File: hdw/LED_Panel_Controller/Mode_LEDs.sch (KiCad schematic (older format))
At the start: 0 parts

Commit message: made a lot more schematic progress
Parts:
- added C? (x9): 0.1uF, Capacitors_SMD:C_0402, symbol Custom_Library:C_Custom
- added D? (x9): Green, LEDs:LED_0402, symbol Device:LED
- added R? (x9): 1k, Resistors_SMD:R_0402, symbol Custom_Library:R_Custom
- added R? (x9): 10k, Resistors_SMD:R_0402, symbol Custom_Library:R_Custom
- added U? (x9): 74LVC1G97, Package_TO_SOT_SMD:SOT-363_SC-70-6, symbol Custom_Library:74LVC1G97_Power_NOT
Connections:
- new net: D?.1 (K), U?.4 (x9)
- new net: D?.2 (A), R?.2 (x9)
- new net +3V3: C?.1, C?.1, C?.1, C?.1, C?.1, C?.1, C?.1, C?.1, C?.1, R?.1, R?.1, R?.1, R?.1, R?.1, R?.1, R?.1, R?.1, R?.1, U?.1 (VCC), U?.1 (VCC), U?.1 (VCC), U?.1 (VCC), U?.1 (VCC), U?.1 (VCC), U?.1 (VCC), U?.1 (VCC), U?.1 (VCC), U?.5 (VCC), U?.5 (VCC), U?.5 (VCC), U?.5 (VCC), U?.5 (VCC), U?.5 (VCC), U?.5 (VCC), U?.5 (VCC), U?.5 (VCC)
- new net Clock_Mode_LED: R?.1, U?.6
- new net Flash_Slideshow_Mode_LED: R?.1, U?.6
- new net GND: C?.2, C?.2, C?.2, C?.2, C?.2, C?.2, C?.2, C?.2, C?.2, R?.2, R?.2, R?.2, R?.2, R?.2, R?.2, R?.2, R?.2, R?.2, U?.2 (GND), U?.2 (GND), U?.2 (GND), U?.2 (GND), U?.2 (GND), U?.2 (GND), U?.2 (GND), U?.2 (GND), U?.2 (GND), U?.3 (GND), U?.3 (GND), U?.3 (GND), U?.3 (GND), U?.3 (GND), U?.3 (GND), U?.3 (GND), U?.3 (GND), U?.3 (GND)
- new net Prog1_Mode_LED: R?.1, U?.6
- new net Prog2_Mode_LED: R?.1, U?.6
- new net Prog3_Mode_LED: R?.1, U?.6
- new net Prog4_Mode_LED: R?.1, U?.6
- new net Prog5_Mode_LED: R?.1, U?.6
- new net Prog6_Mode_LED: R?.1, U?.6
- new net USB_Stream_Mode_LED: R?.1, U?.6

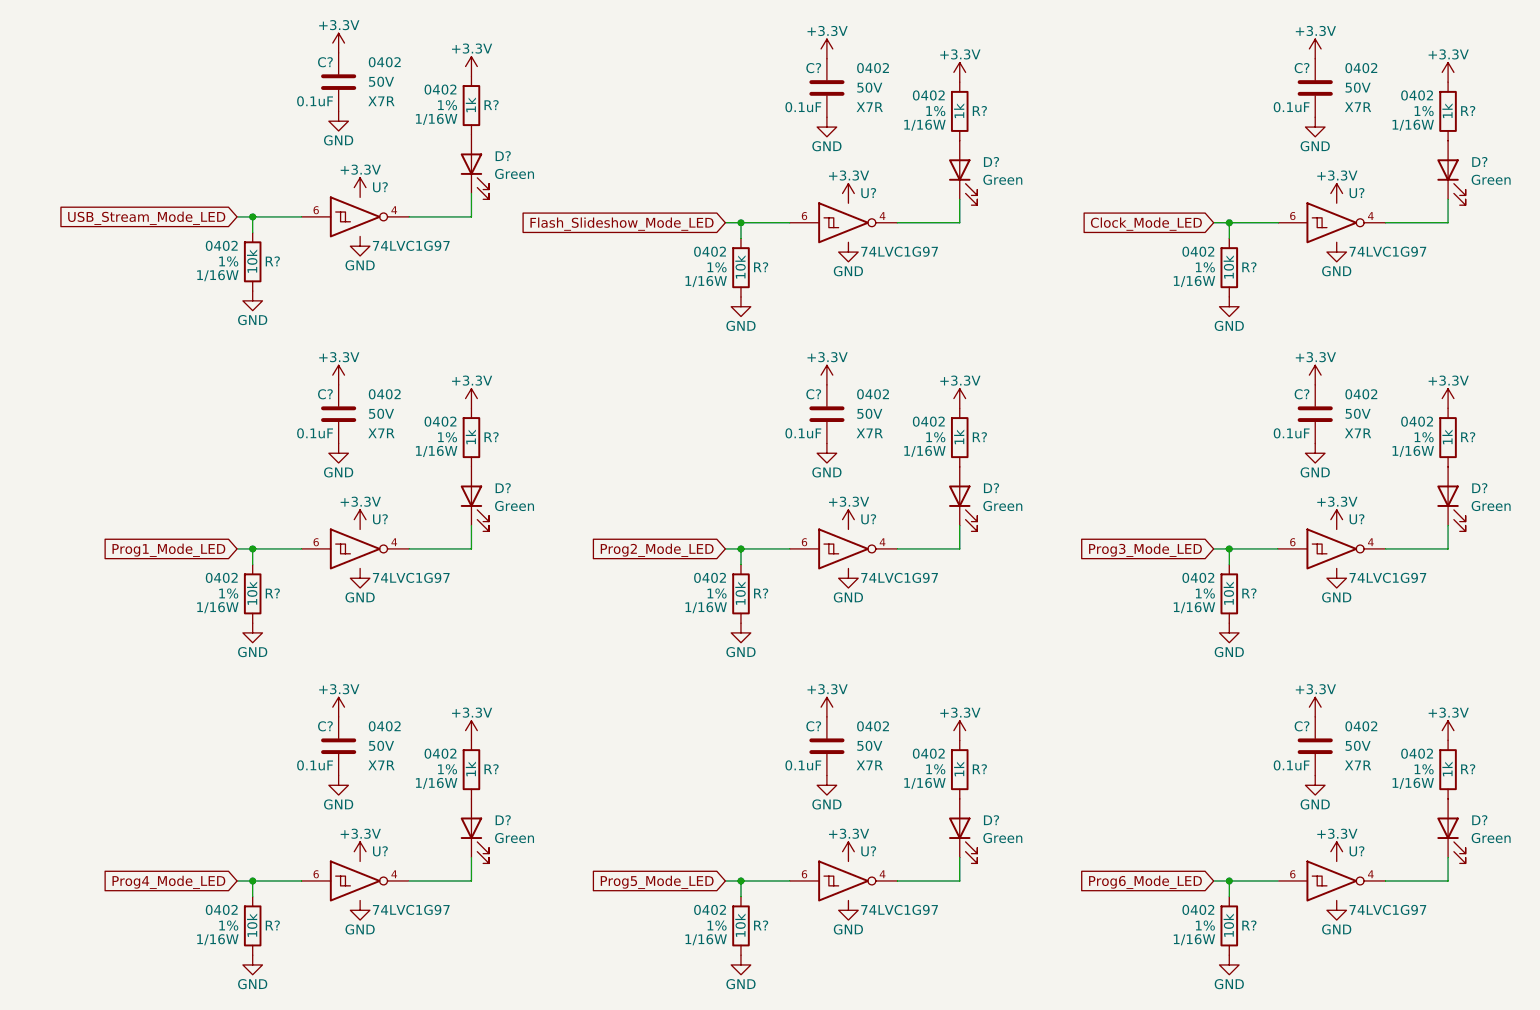
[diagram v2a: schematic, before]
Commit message: assigned a lot of nets to MCU pins
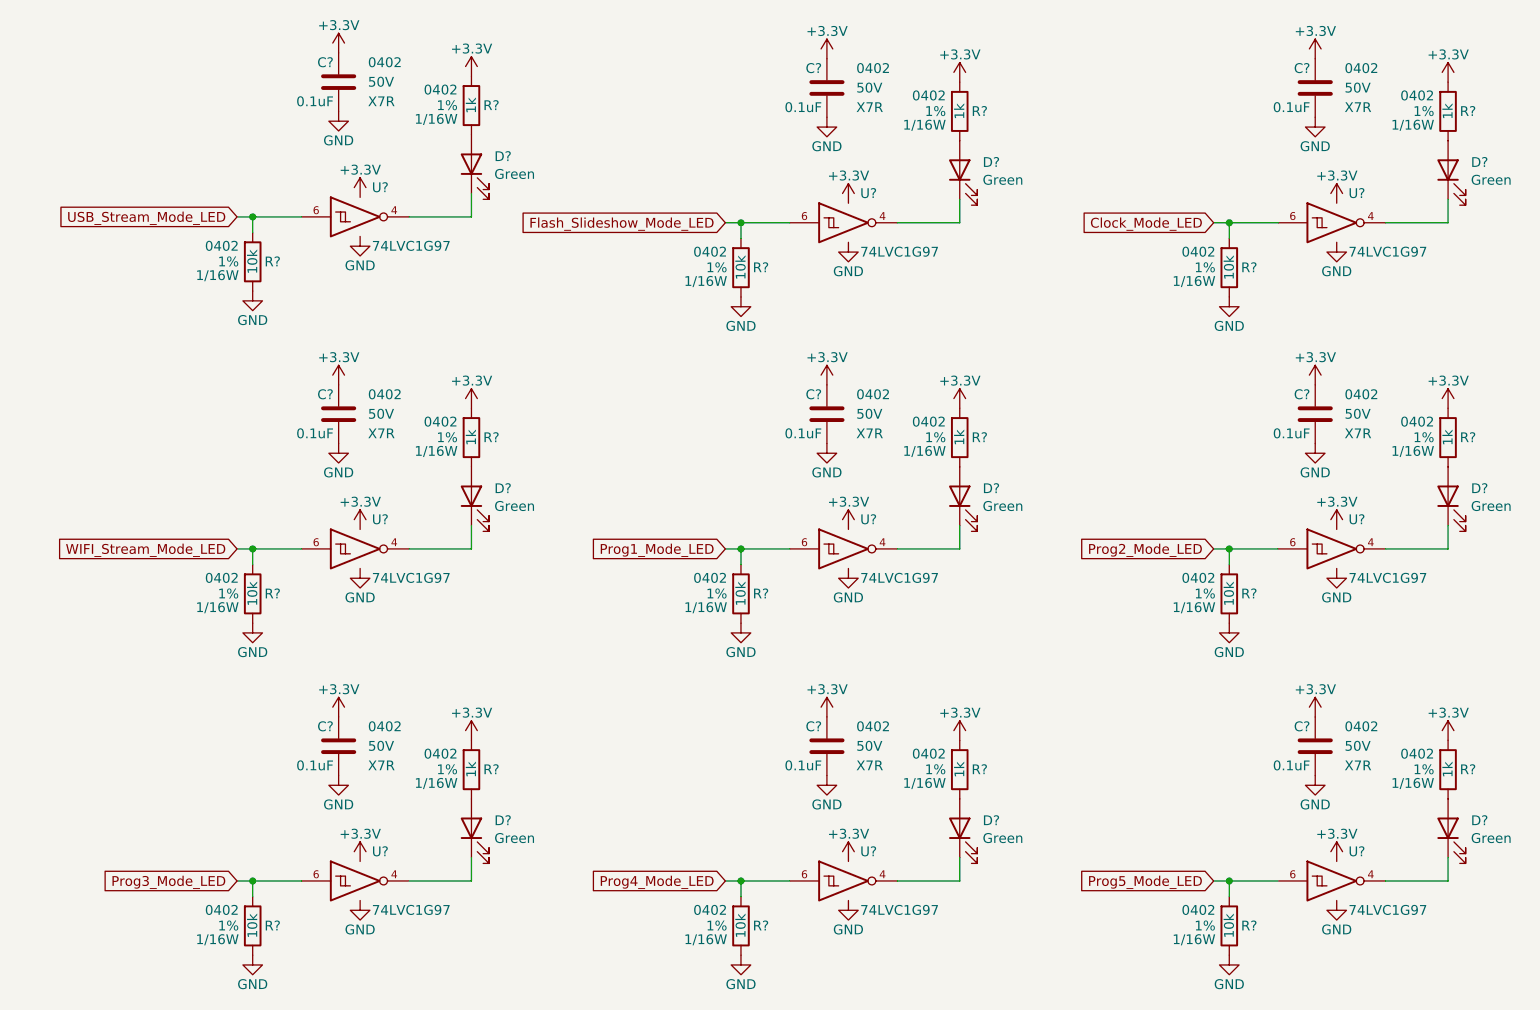
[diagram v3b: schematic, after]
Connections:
- net Prog6_Mode_LED is gone; now on net Prog5_Mode_LED: R?.1, U?.6
- net Prog1_Mode_LED: now also R?.1, U?.6; no longer R?.1, U?.6
- net Prog2_Mode_LED: now also R?.1, U?.6; no longer R?.1, U?.6
- net Prog3_Mode_LED: now also R?.1, U?.6; no longer R?.1, U?.6
- net Prog4_Mode_LED: now also R?.1, U?.6; no longer R?.1, U?.6
- net Prog5_Mode_LED: no longer R?.1, U?.6
- new net WIFI_Stream_Mode_LED: R?.1, U?.6
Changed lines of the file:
@@
 $EndComp
 Text GLabel 1560 3460 0    50   Input ~ 0
-Prog1_Mode_LED
+WIFI_Stream_Mode_LED
 $Comp
 L Custom_Library:C_Custom C?
@@
 $EndComp
 Text GLabel 4060 3460 0    50   Input ~ 0
-Prog2_Mode_LED
+Prog1_Mode_LED
 $Comp
 L Custom_Library:C_Custom C?
@@
 $EndComp
 Text GLabel 6560 3460 0    50   Input ~ 0
-Prog3_Mode_LED
+Prog2_Mode_LED
 $Comp
 L Custom_Library:C_Custom C?
@@
 $EndComp
 Text GLabel 1560 5160 0    50   Input ~ 0
-Prog4_Mode_LED
+Prog3_Mode_LED
 $Comp
 L Custom_Library:C_Custom C?
@@
 $EndComp
 Text GLabel 4060 5160 0    50   Input ~ 0
-Prog5_Mode_LED
+Prog4_Mode_LED
 $Comp
 L Custom_Library:C_Custom C?
@@
 $EndComp
 Text GLabel 6560 5160 0    50   Input ~ 0
-Prog6_Mode_LED
+Prog5_Mode_LED
 $Comp
 L Custom_Library:C_Custom C?

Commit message: more schematic development
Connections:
- net Clock_Mode_LED renamed Void_Mode_LED
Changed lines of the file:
@@
 $Descr A 11000 8500
 encoding utf-8
-Sheet 22 34
+Sheet 23 34
 Title "LED Panel Controller"
-Date "2020-12-23"
+Date "2021-03-24"
 Rev "A"
-Comp "Drew Maatman, Logan Wedel"
+Comp "Drew Maatman"
 Comment1 ""
 Comment2 ""
@@
 	6640 1790 6640 1870
 Text GLabel 6560 1790 0    50   Input ~ 0
-Clock_Mode_LED
+Void_Mode_LED
 Wire Wire Line
 	6560 1790 6640 1790

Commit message: added digikey pns, footprints, bom scrubbed
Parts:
- R? (x9): Digi-Key PN (none) -> RMCF0402FT1K00CT-ND
- U? (x9): Digi-Key PN (none) -> 1727-1772-1-ND
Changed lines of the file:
@@
 F 5 "1%" H 2830 1190 50  0000 L CNN "Tolerance"
 F 6 "1/16W" H 2830 1120 50  0000 L CNN "Wattage"
-F 7 "" H 3060 1590 60  0001 C CNN "Digi-Key PN"
+F 7 "RMCF0402FT1K00CT-ND" H 3060 1590 60  0001 C CNN "Digi-Key PN"
 	1    2760 1190
 	-1   0    0    -1
@@
 F 2 "Package_TO_SOT_SMD:SOT-363_SC-70-6" H 2240 1760 50  0001 C CNN
 F 3 "http://www.ti.com/lit/ds/symlink/sn74lvc1g97.pdf" H 2240 1760 50  0001 C CNN
+F 4 "1727-1772-1-ND" H 2190 1760 50  0001 C CNN "Digi-Key PN"
 	1    2190 1760
 	1    0    0    -1
@@
 F 5 "1%" H 5330 1220 50  0000 L CNN "Tolerance"
 F 6 "1/16W" H 5330 1150 50  0000 L CNN "Wattage"
-F 7 "" H 5560 1620 60  0001 C CNN "Digi-Key PN"
+F 7 "RMCF0402FT1K00CT-ND" H 5560 1620 60  0001 C CNN "Digi-Key PN"
 	1    5260 1220
 	-1   0    0    -1
@@
 F 2 "Package_TO_SOT_SMD:SOT-363_SC-70-6" H 4740 1790 50  0001 C CNN
 F 3 "http://www.ti.com/lit/ds/symlink/sn74lvc1g97.pdf" H 4740 1790 50  0001 C CNN
+F 4 "1727-1772-1-ND" H 4690 1790 50  0001 C CNN "Digi-Key PN"
 	1    4690 1790
 	1    0    0    -1
@@
 F 5 "1%" H 2830 2890 50  0000 L CNN "Tolerance"
 F 6 "1/16W" H 2830 2820 50  0000 L CNN "Wattage"
-F 7 "" H 3060 3290 60  0001 C CNN "Digi-Key PN"
+F 7 "RMCF0402FT1K00CT-ND" H 3060 3290 60  0001 C CNN "Digi-Key PN"
 	1    2760 2890
 	-1   0    0    -1
@@
 F 2 "Package_TO_SOT_SMD:SOT-363_SC-70-6" H 2240 3460 50  0001 C CNN
 F 3 "http://www.ti.com/lit/ds/symlink/sn74lvc1g97.pdf" H 2240 3460 50  0001 C CNN
+F 4 "1727-1772-1-ND" H 2190 3460 50  0001 C CNN "Digi-Key PN"
 	1    2190 3460
 	1    0    0    -1
@@
 F 5 "1%" H 5330 2890 50  0000 L CNN "Tolerance"
 F 6 "1/16W" H 5330 2820 50  0000 L CNN "Wattage"
-F 7 "" H 5560 3290 60  0001 C CNN "Digi-Key PN"
+F 7 "RMCF0402FT1K00CT-ND" H 5560 3290 60  0001 C CNN "Digi-Key PN"
 	1    5260 2890
 	-1   0    0    -1
@@
 F 2 "Package_TO_SOT_SMD:SOT-363_SC-70-6" H 4740 3460 50  0001 C CNN
 F 3 "http://www.ti.com/lit/ds/symlink/sn74lvc1g97.pdf" H 4740 3460 50  0001 C CNN
+F 4 "1727-1772-1-ND" H 4690 3460 50  0001 C CNN "Digi-Key PN"
 	1    4690 3460
 	1    0    0    -1
@@
 F 5 "1%" H 7830 2890 50  0000 L CNN "Tolerance"
 F 6 "1/16W" H 7830 2820 50  0000 L CNN "Wattage"
-F 7 "" H 8060 3290 60  0001 C CNN "Digi-Key PN"
+F 7 "RMCF0402FT1K00CT-ND" H 8060 3290 60  0001 C CNN "Digi-Key PN"
 	1    7760 2890
 	-1   0    0    -1
@@
 F 2 "Package_TO_SOT_SMD:SOT-363_SC-70-6" H 7240 3460 50  0001 C CNN
 F 3 "http://www.ti.com/lit/ds/symlink/sn74lvc1g97.pdf" H 7240 3460 50  0001 C CNN
+F 4 "1727-1772-1-ND" H 7190 3460 50  0001 C CNN "Digi-Key PN"
 	1    7190 3460
 	1    0    0    -1
@@
 F 5 "1%" H 2830 4590 50  0000 L CNN "Tolerance"
 F 6 "1/16W" H 2830 4520 50  0000 L CNN "Wattage"
-F 7 "" H 3060 4990 60  0001 C CNN "Digi-Key PN"
+F 7 "RMCF0402FT1K00CT-ND" H 3060 4990 60  0001 C CNN "Digi-Key PN"
 	1    2760 4590
 	-1   0    0    -1
@@
 F 2 "Package_TO_SOT_SMD:SOT-363_SC-70-6" H 2240 5160 50  0001 C CNN
 F 3 "http://www.ti.com/lit/ds/symlink/sn74lvc1g97.pdf" H 2240 5160 50  0001 C CNN
+F 4 "1727-1772-1-ND" H 2190 5160 50  0001 C CNN "Digi-Key PN"
 	1    2190 5160
 	1    0    0    -1
@@
 F 5 "1%" H 5330 4590 50  0000 L CNN "Tolerance"
 F 6 "1/16W" H 5330 4520 50  0000 L CNN "Wattage"
-F 7 "" H 5560 4990 60  0001 C CNN "Digi-Key PN"
+F 7 "RMCF0402FT1K00CT-ND" H 5560 4990 60  0001 C CNN "Digi-Key PN"
 	1    5260 4590
 	-1   0    0    -1
@@
 F 2 "Package_TO_SOT_SMD:SOT-363_SC-70-6" H 4740 5160 50  0001 C CNN
 F 3 "http://www.ti.com/lit/ds/symlink/sn74lvc1g97.pdf" H 4740 5160 50  0001 C CNN
+F 4 "1727-1772-1-ND" H 4690 5160 50  0001 C CNN "Digi-Key PN"
 	1    4690 5160
 	1    0    0    -1
@@
 F 5 "1%" H 7830 4590 50  0000 L CNN "Tolerance"
 F 6 "1/16W" H 7830 4520 50  0000 L CNN "Wattage"
-F 7 "" H 8060 4990 60  0001 C CNN "Digi-Key PN"
+F 7 "RMCF0402FT1K00CT-ND" H 8060 4990 60  0001 C CNN "Digi-Key PN"
 	1    7760 4590
 	-1   0    0    -1
@@
 F 2 "Package_TO_SOT_SMD:SOT-363_SC-70-6" H 7240 5160 50  0001 C CNN
 F 3 "http://www.ti.com/lit/ds/symlink/sn74lvc1g97.pdf" H 7240 5160 50  0001 C CNN
+F 4 "1727-1772-1-ND" H 7190 5160 50  0001 C CNN "Digi-Key PN"
 	1    7190 5160
 	1    0    0    -1
@@
 F 5 "1%" H 7830 1220 50  0000 L CNN "Tolerance"
 F 6 "1/16W" H 7830 1150 50  0000 L CNN "Wattage"
-F 7 "" H 8060 1620 60  0001 C CNN "Digi-Key PN"
+F 7 "RMCF0402FT1K00CT-ND" H 8060 1620 60  0001 C CNN "Digi-Key PN"
 	1    7760 1220
 	-1   0    0    -1
@@
 F 2 "Package_TO_SOT_SMD:SOT-363_SC-70-6" H 7240 1790 50  0001 C CNN
 F 3 "http://www.ti.com/lit/ds/symlink/sn74lvc1g97.pdf" H 7240 1790 50  0001 C CNN
+F 4 "1727-1772-1-ND" H 7190 1790 50  0001 C CNN "Digi-Key PN"
 	1    7190 1790
 	1    0    0    -1

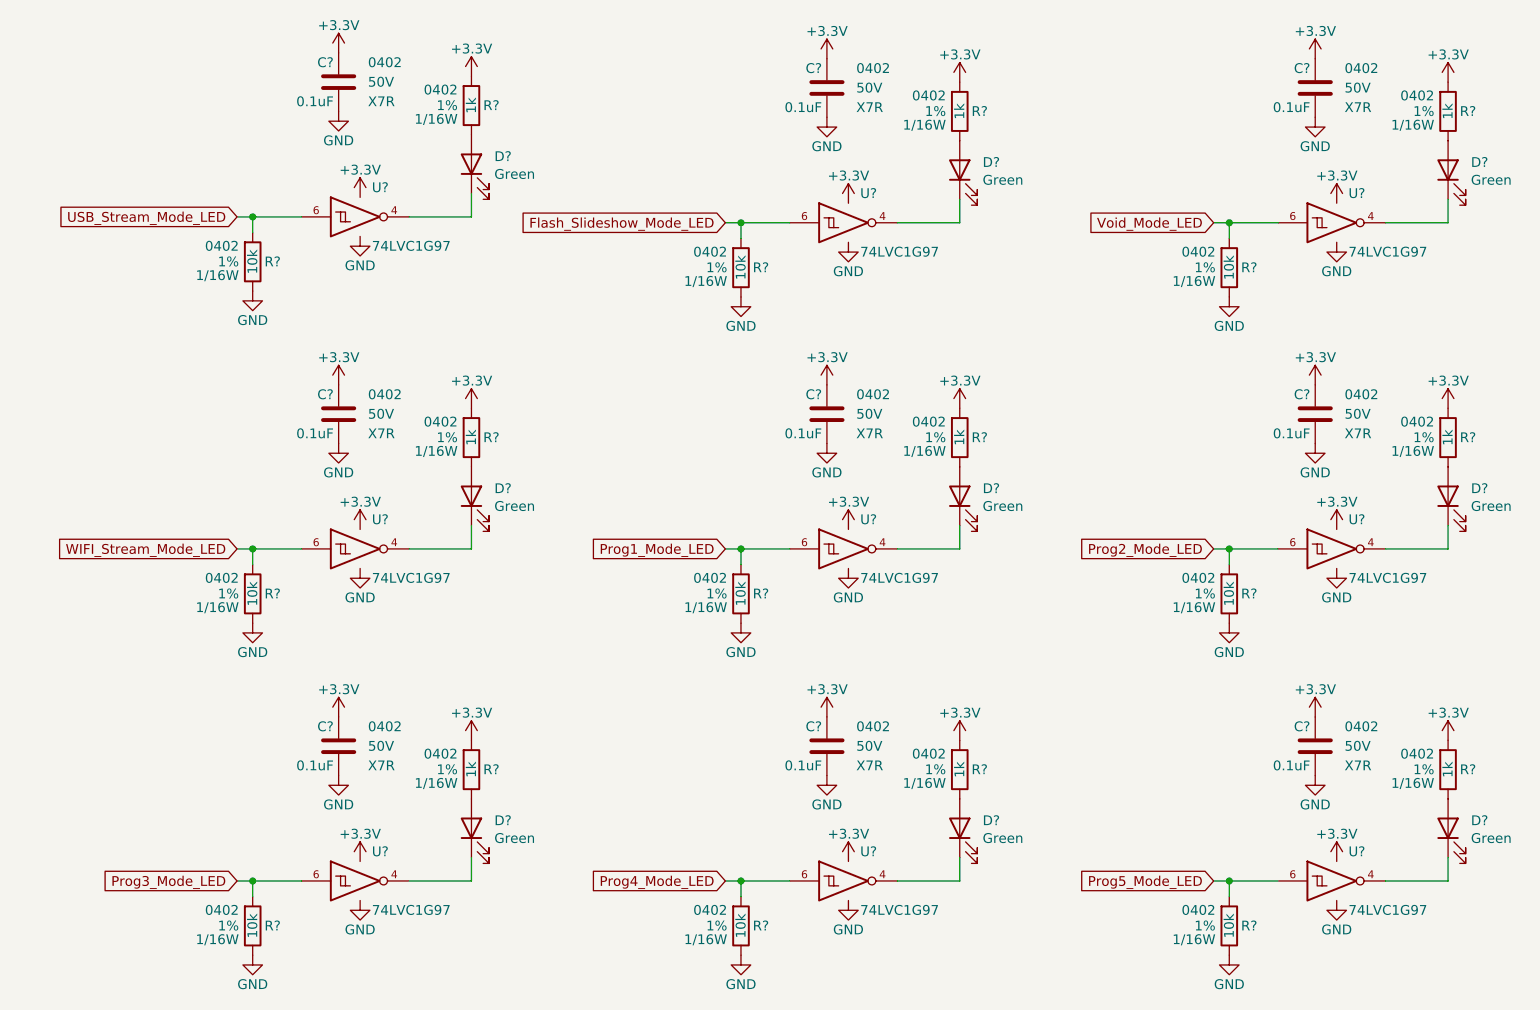
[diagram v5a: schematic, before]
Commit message: assigned I2C addresses
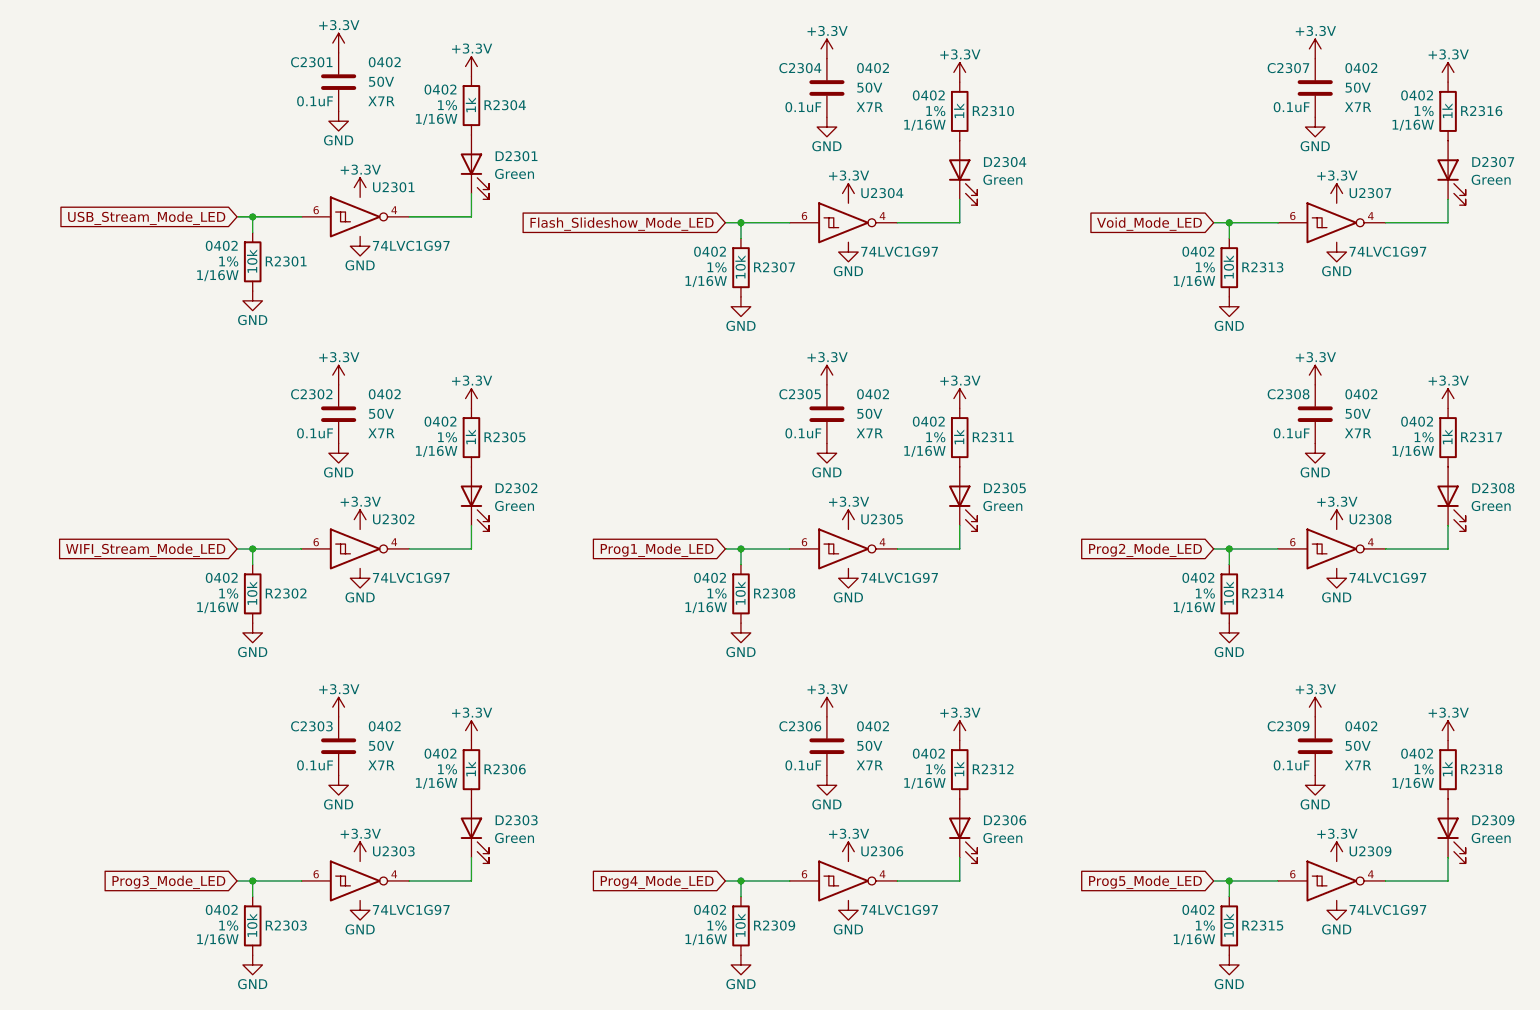
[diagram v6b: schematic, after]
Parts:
- gave numbers to parts that had none: 45
